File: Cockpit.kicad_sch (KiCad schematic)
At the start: 0 parts

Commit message: cockpit done
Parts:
- added C25, C27, C29, C30, C31, C32: 100nF, Capacitor_SMD:C_0603_1608Metric, symbol Device:C
- added C26, C28, C33, C34: 22pF, Capacitor_SMD:C_0603_1608Metric, symbol Device:C
- added D2: PI_DEG_A_BLUE, LED_THT:LED_D3.0mm, symbol Device:LED
- added D3: PI_DEG_B_BLUE, LED_THT:LED_D3.0mm, symbol Device:LED
- added D4: PI_ERROR_RED, LED_THT:LED_D3.0mm, symbol Device:LED
- added J2: PI_GPIO_40, Connector_PinHeader_2.54mm:PinHeader_2x20_P2.54mm_Vertical, symbol Connector_Generic:Conn_02x20_Odd_Even
- added J3: CAN_A_PROBE, Connector_PinHeader_2.54mm:PinHeader_1x02_P2.54mm_Vertical, symbol Connector_Generic:Conn_01x02
- added J4: CAN_B_PROBE, Connector_PinHeader_2.54mm:PinHeader_1x02_P2.54mm_Vertical, symbol Connector_Generic:Conn_01x02
- added R17, R18, R20, R21: 10k, Resistor_SMD:R_0603_1608Metric, symbol Device:R
- added R19, R22: 120R, Resistor_SMD:R_0603_1608Metric, symbol Device:R
- added R23, R24, R25: 220R, Resistor_SMD:R_0603_1608Metric, symbol Device:R
- added S1: PI_SELF_TEST, SWT0210-045026GSA:SW_SWT0210-045026GSA_REVA, symbol SWT0210-045026GSA:SWT0210-045026GSA_REVA
- added SW1, SW3: 219-2MSTR, Button_Switch_SMD:SW_DIP_SPSTx02_Slide_6.7x6.64mm_W8.61mm_P2.54mm_LowProfile, symbol Switch:SW_DIP_x02
- added SW2, SW4: CVS-01TB, Button_Switch_SMD:SW_DIP_SPSTx01_Slide_Copal_CVS-01xB_W5.9mm_P1mm, symbol Switch:SW_DIP_x01
- added TP1, TP10, TP11, TP12, TP2, TP3, TP4, TP5, TP6, TP7, TP8, TP9: 5015, TestPoint:TestPoint_Keystone_5015_Micro_Mini, symbol Connector:TestPoint
- added U4, U6: MCP2515T-I/ST, Package_SO:TSSOP-20_4.4x6.5mm_P0.65mm, symbol Interface_CAN_LIN:MCP2515-xST
- added U5, U7: SN65HVD230, Package_SO:SOIC-8_3.9x4.9mm_P1.27mm, symbol Interface_CAN_LIN:SN65HVD230
- added W1: 40-pin Pi GPIO ribbon cable, symbol Mechanical:Housing
- added Y1, Y2: 16 MHz, Crystal:Crystal_SMD_3225-4Pin_3.2x2.5mm, symbol Device:Crystal_GND24
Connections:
- new net: U4.1 (TXCAN), U5.1 (D)
- new net: C27.1, R17.1, U4.19 (~{RESET})
- new net: U4.2 (RXCAN), U5.4 (R)
- new net: R19.1, SW2.1
- new net: C31.1, R20.1, U6.19 (~{RESET})
- new net: D2.2 (A), R24.2
- new net: R22.1, SW4.1
- new net: D3.2 (A), R23.2
- new net: SW1.1, U5.7 (CANH)
- new net: SW1.2, U5.6 (CANL)
- new net: SW3.1, U7.7 (CANH)
- new net: SW3.2, U7.6 (CANL)
- new net: U6.1 (TXCAN), U7.1 (D)
- new net: U6.2 (RXCAN), U7.4 (R)
- new net: R18.2, U5.8 (Rs)
- new net: R21.2, U7.8 (Rs)
- new net: D4.2 (A), R25.2
- new net 3V3: C25.1, C29.1, C30.1, C32.1, R17.2, R20.2, U4.20 (VDD), U5.3 (VCC), U6.20 (VDD), U7.3 (VCC)
- new net 5V: J2.2 (Pin_2), J2.4 (Pin_4)
- new net CANH_A: R19.2, SW1.4
- new net CANH_B: J4.1 (Pin_1), R22.2, SW3.4
- new net CANL_A: SW1.3, SW2.2
- new net CANL_B: J4.2 (Pin_2), SW3.3, SW4.2
- new net CAN_RX_A: J2.35 (Pin_35), TP6.1
- new net CAN_RX_B: J2.36 (Pin_36), TP8.1
- new net CAN_TX_A: J2.32 (Pin_32), TP7.1
- new net CAN_TX_B: J2.33 (Pin_33), TP5.1
- new net CMD_TX: J2.31 (Pin_31), TP4.1
- new net GND: C25.2, C26.2, C27.2, C28.2, C29.2, C30.2, C31.2, C32.2, C33.2, C34.2, D2.1 (K), D3.1 (K), D4.1 (K), J2.14 (Pin_14), J2.20 (Pin_20), J2.25 (Pin_25), J2.30 (Pin_30), J2.34 (Pin_34), J2.39 (Pin_39), J2.6 (Pin_6), J2.9 (Pin_9), R18.1, R21.1, S1.1, TP1.1, TP2.1, U4.10 (VSS), U5.2 (GND), U6.10 (VSS), U7.2 (GND), Y1.2 (G), Y1.4 (G), Y2.2 (G), Y2.4 (G)
- new net OSC_PI_A1: C26.1, U4.9 (OSC1), Y1.1
- new net OSC_PI_A2: C28.1, U4.8 (OSC2), Y1.3
- new net OSC_PI_B1: C33.1, U6.8 (OSC2), Y2.1
- new net OSC_PI_B2: C34.1, U6.9 (OSC1), Y2.3
- new net PI_CAN_A_CS: J2.24 (Pin_24), U4.18 (~{CS})
- new net PI_CAN_A_INT: J2.22 (Pin_22), U4.13 (~{INT})
- new net PI_CAN_B_CS: J2.26 (Pin_26), U6.18 (~{CS})
- new net PI_CAN_B_INT: J2.18 (Pin_18), U6.13 (~{INT})
- new net PI_DEG_A_LED: J2.13 (Pin_13), R24.1, TP9.1
- new net PI_DEG_B_LED: J2.15 (Pin_15), R23.1, TP10.1
- new net PI_ERR_LED: J2.16 (Pin_16), R25.1, TP11.1
- new net PI_SELF_TEST: J2.11 (Pin_11), S1.3, TP12.1
- new net PI_SPI_MISO: J2.21 (Pin_21), U4.17 (SO), U6.17 (SO)
- new net PI_SPI_MOSI: J2.19 (Pin_19), U4.16 (SI), U6.16 (SI)
- new net PI_SPI_SCLK: J2.23 (Pin_23), U4.14 (SCK), U6.14 (SCK)
- new net UDP_RX: J2.29 (Pin_29), TP3.1
- no-connect marks 0 -> 29
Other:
- note added: "Battery Input"
- note added: "CAN A Interface"
- note added: "CAN B Interface"
- note added: "Only one probe header per CAN bus is needed."
- note added: "Pi connection: J2 connects to the Raspberry Pi 4 GPIO header using one 40-pin, 2×20 female-to-female ribbon cable. Buy Adafruit 1988, DigiKey 1528-2235-ND. Align pin 1 at both ends before powering on."
- note added: "Self Test and status LEDs"

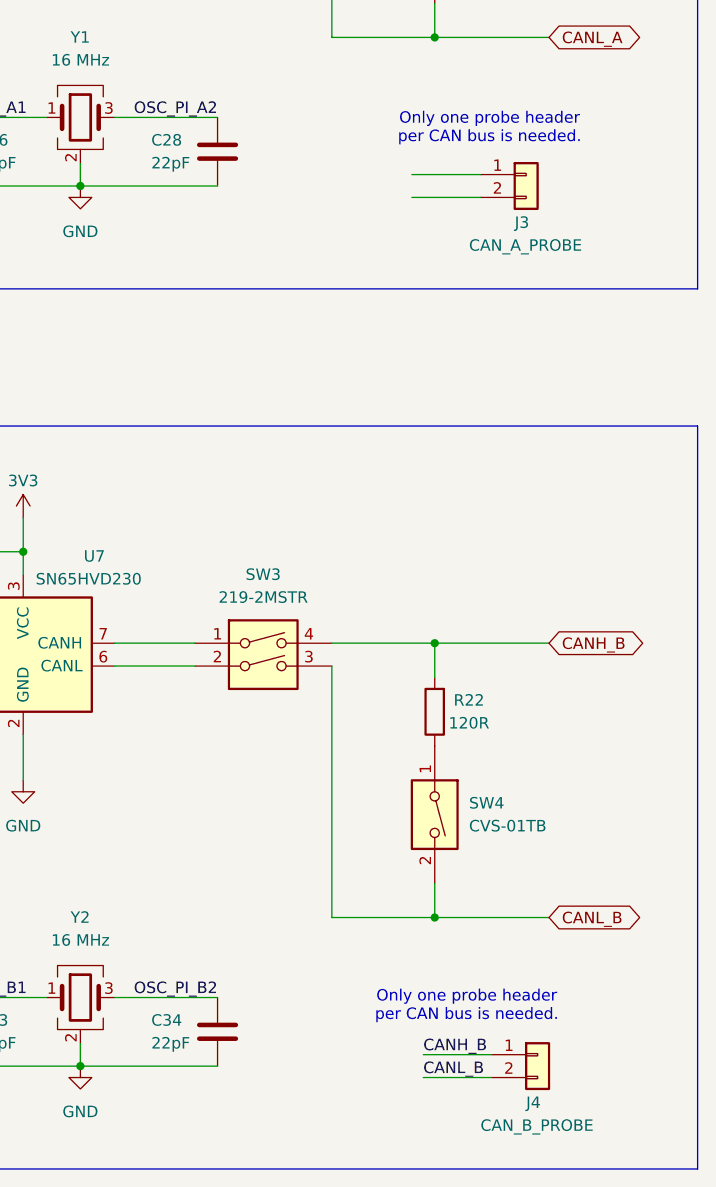
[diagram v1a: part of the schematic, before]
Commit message: Drivetrain: STM32 core, dual CAN, LEDs, self-test, test points, footprints
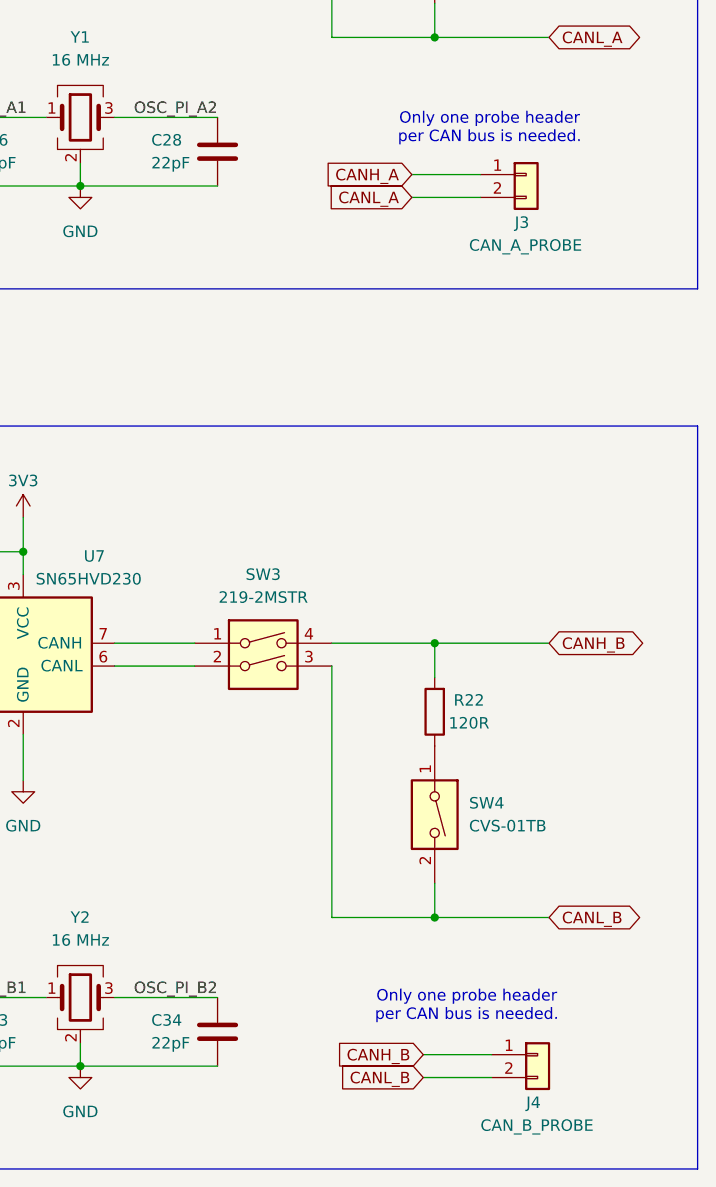
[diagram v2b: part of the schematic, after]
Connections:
- net CANH_A: now also J3.1 (Pin_1)
- net CANL_A: now also J3.2 (Pin_2)
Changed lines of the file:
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@@
-		)
-	)
-	(label "CANL_B"
-		(at 337.82 222.25 0)
-		(effects
-			(font
-				(size 1.27 1.27)
-			)
-			(justify left bottom)
 		)
 	)
@@
 	(label "CMD_TX"
 		(at 59.69 105.41 0)
-		(effects
-			(font
-				(size 1.27 1.27)
-			)
-			(justify left bottom)
-		)
-	)
-	(label "CANH_B"
-		(at 337.82 219.71 0)
 		(effects
 			(font
@@
 		)
 	)
+	(global_label "CANH_B"
+		(shape input)
+		(at 337.82 219.71 180)
+		(fields_autoplaced yes)
+		(effects
+			(font
+				(size 1.27 1.27)
+			)
+			(justify right)
+		)
+		(property "Intersheetrefs" "${INTERSHEET_REFS}"
+			(at 327.5776 219.71 0)
+			(hide yes)
+			(show_name no)
+			(do_not_autoplace no)
+			(effects
+				(font
+					(size 1.27 1.27)
+				)
+				(justify right)
+			)
+		)
+	)
 	(global_label "CANH_A"
 		(shape bidirectional)
@@
 			)
 		)
+	)
+	(global_label "CANL_B"
+		(shape input)
+		(at 337.82 222.25 180)
+		(fields_autoplaced yes)
+		(effects
+			(font
+				(size 1.27 1.27)
+			)
+			(justify right)
+		)
+		(property "Intersheetrefs" "${INTERSHEET_REFS}"
+			(at 327.88 222.25 0)
+			(hide yes)
+			(show_name no)
+			(do_not_autoplace no)
+			(effects
+				(font
+					(size 1.27 1.27)
+				)
+				(justify right)
+			)
+		)
+	)
+	(global_label "CANH_A"
+		(shape input)
+		(at 336.55 121.92 180)
+		(fields_autoplaced yes)
+		(effects
+			(font
+				(size 1.27 1.27)
+			)
+			(justify right)
+		)
+		(property "Intersheetrefs" "${INTERSHEET_REFS}"
+			(at 326.489 121.92 0)
+			(hide yes)
+			(show_name no)
+			(do_not_autoplace no)
+			(effects
+				(font
+					(size 1.27 1.27)
+				)
+				(justify right)
+			)
+		)
+	)
+	(global_label "CANL_A"
+		(shape input)
+		(at 336.55 124.46 180)
+		(fields_autoplaced yes)
+		(effects
+			(font
+				(size 1.27 1.27)
+			)
+			(justify right)
+		)
+		(property "Intersheetrefs" "${INTERSHEET_REFS}"
+			(at 326.7914 124.46 0)
+			(hide yes)
+			(show_name no)
+			(do_not_autoplace no)
+			(effects
+				(font
+					(size 1.27 1.27)
+				)
+				(justify right)
+			)
+		)

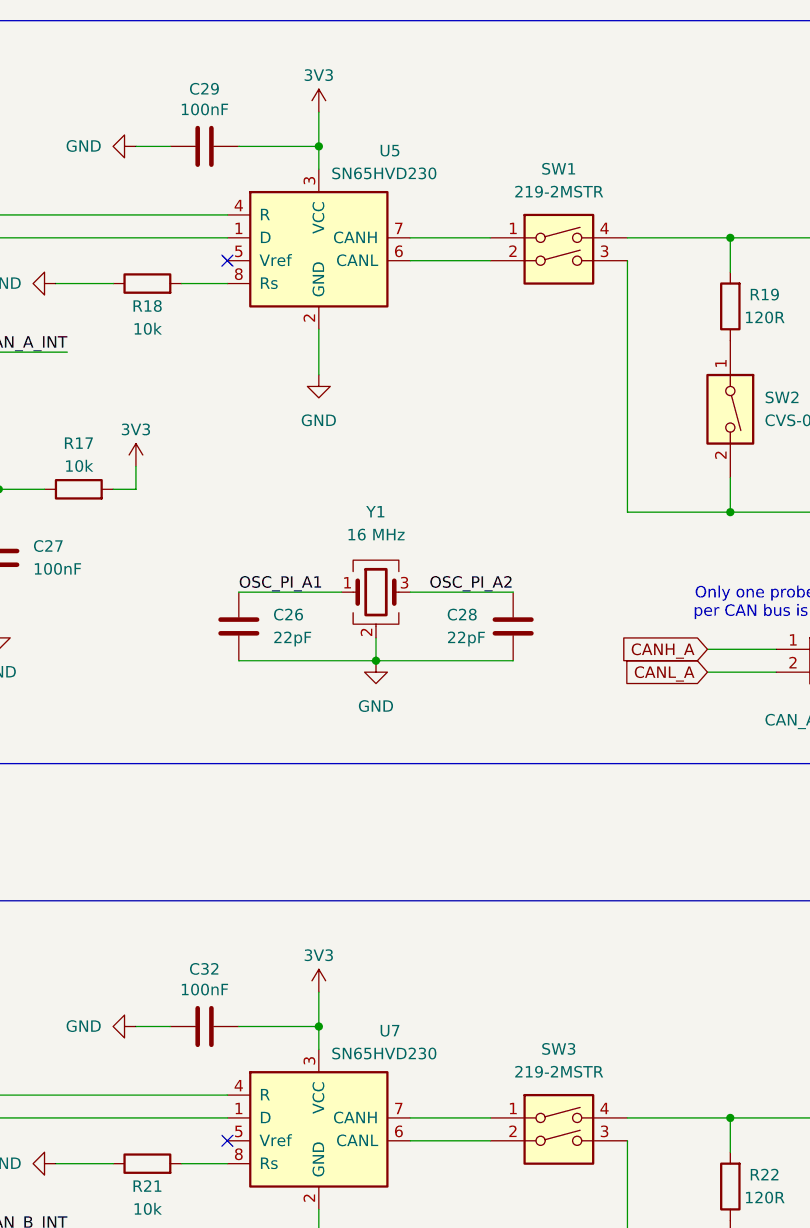
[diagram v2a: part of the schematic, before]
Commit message: changed MPN on CAN
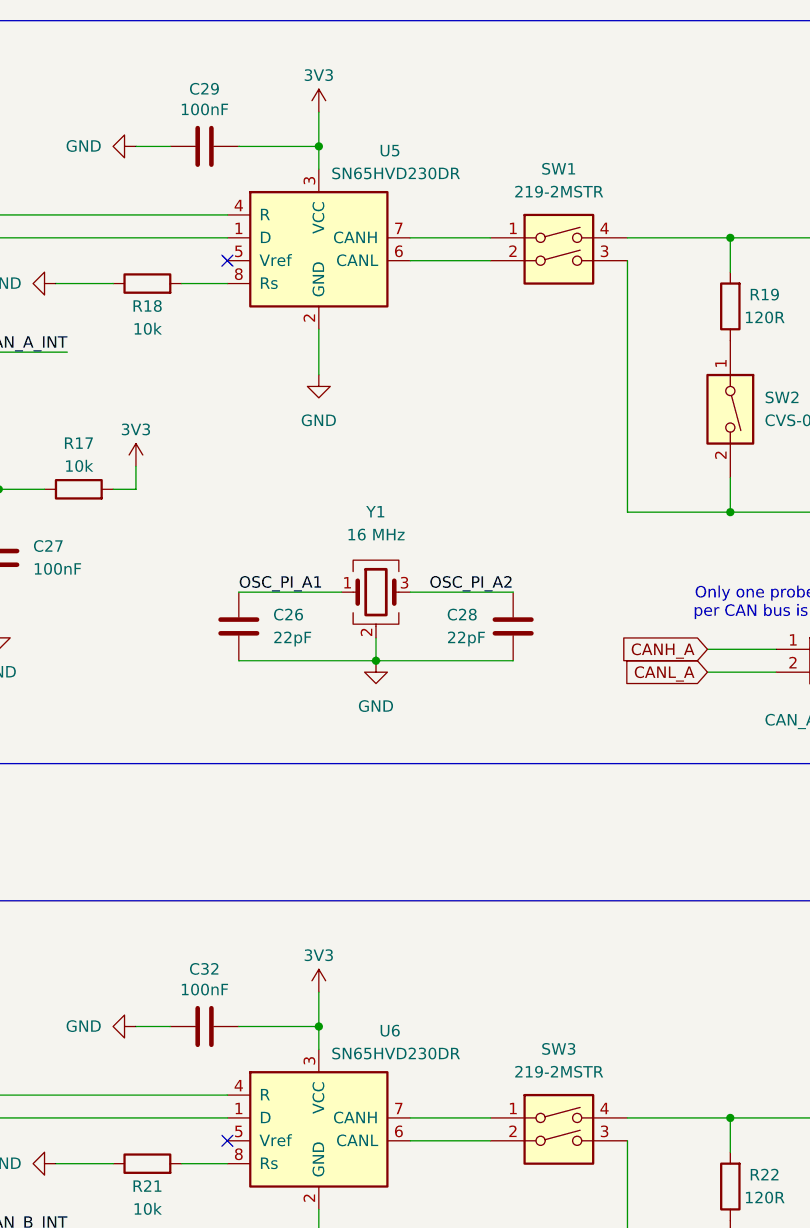
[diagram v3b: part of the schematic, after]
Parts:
- removed U7: SN65HVD230, Package_SO:SOIC-8_3.9x4.9mm_P1.27mm, symbol Interface_CAN_LIN:SN65HVD230
- added U6: SN65HVD230DR, Package_SO:SOIC-8_3.9x4.9mm_P1.27mm, symbol Interface_CAN_LIN:SN65HVD230
- U5: value SN65HVD230 -> SN65HVD230DR; Assembly (none) -> SMT; JLCPCB Category (none) -> Extended; LCSC Part # (none) -> C12084; Manufacturer (none) -> Texas Instruments; Manufacturer Part Number (none) -> SN65HVD230DR; Source (none) -> JLCPCB
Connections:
- net 3V3: now also U6.3 (VCC)
- net GND: now also U6.2 (GND)
- net at SW3.1: now also U6.7 (CANH)
- net at SW3.2: now also U6.6 (CANL)
- net at U6.1 (TXCAN): now also U6.1 (D)
- net at U6.2 (RXCAN): now also U6.4 (R)
- net at R21.2: now also U6.8 (Rs)
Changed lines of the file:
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@@
 			)
 		)
-		(property "Value" "SN65HVD230"
+		(property "Value" "SN65HVD230DR"
 			(at 294.7513 69.088 0)
 			(show_name no)
@@
 			)
 		)
-		(property "Manufacturer" ""
+		(property "Manufacturer" "Texas Instruments"
 			(at 293.37 76.2 0)
 			(hide yes)
@@
 			)
 		)
-		(property "Manufacturer Part Number" ""
+		(property "Manufacturer Part Number" "SN65HVD230DR"
 			(at 293.37 76.2 0)
 			(hide yes)
@@
 			)
 		)
-		(property "Source" ""
+		(property "Source" "JLCPCB"
 			(at 293.37 76.2 0)
 			(hide yes)
@@
 			)
 		)
-		(property "Assembly" ""
+		(property "Assembly" "SMT"
 			(at 293.37 76.2 0)
 			(hide yes)
@@
 			)
 		)
-		(property "LCSC Part #" ""
+		(property "LCSC Part #" "C12084"
 			(at 293.37 76.2 0)
 			(hide yes)
@@
 			)
 		)
-		(property "JLCPCB Category" ""
+		(property "JLCPCB Category" "Extended"
 			(at 293.37 76.2 0)
 			(hide yes)
@@
 	)
 	(symbol
+		(lib_id "Interface_CAN_LIN:SN65HVD230")
+		(at 293.37 173.99 0)
+		(unit 1)
+		(body_style 1)
+		(exclude_from_sim no)
+		(in_bom yes)
+		(on_board yes)
+		(in_pos_files yes)
+		(dnp no)
+		(property "Reference" "U6"
+			(at 300.0853 164.338 0)
+			(show_name no)
+			(do_not_autoplace no)
+			(effects
+				(font
+					(size 1.27 1.27)
+				)
+				(justify left)
+			)
+		)
+		(property "Value" "SN65HVD230DR"
+			(at 294.7513 166.878 0)
+			(show_name no)
+			(do_not_autoplace no)
+			(effects
+				(font
+					(size 1.27 1.27)
+				)
+				(justify left)
+			)
+		)
+		(property "Footprint" "Package_SO:SOIC-8_3.9x4.9mm_P1.27mm"
+			(at 293.37 186.69 0)
+			(hide yes)
+			(show_name no)
+			(do_not_autoplace no)
+			(effects
+				(font
+					(size 1.27 1.27)
+				)
+			)
+		)
+		(property "Datasheet" "http://www.ti.com/lit/ds/symlink/sn65hvd230.pdf"
+			(at 290.83 163.83 0)
+			(hide yes)
+			(show_name no)
+			(do_not_autoplace no)
+			(effects
+				(font
+					(size 1.27 1.27)
+				)
+			)
+		)
+		(property "Description" "CAN Bus Transceivers, 3.3V, 1Mbps, Low-Power capabilities, SOIC-8"
+			(at 293.37 173.99 0)
+			(hide yes)
+			(show_name no)
+			(do_not_autoplace no)
+			(effects
+				(font
+					(size 1.27 1.27)
+				)
+			)
+		)
+		(property "Manufacturer" "Texas Instruments"
+			(at 293.37 173.99 0)
+			(hide yes)
+			(show_name no)
+			(do_not_autoplace no)
+			(effects
+				(font
+					(size 1.27 1.27)
+				)
+			)
+		)
+		(property "Manufacturer Part Number" "SN65HVD230DR"
+			(at 293.37 173.99 0)
+			(hide yes)
+			(show_name no)
+			(do_not_autoplace no)
+			(effects
+				(font
+					(size 1.27 1.27)
+				)
+			)
+		)
+		(property "Source" "JLCPCB"
+			(at 293.37 173.99 0)
+			(hide yes)
+			(show_name no)
+			(do_not_autoplace no)
+			(effects
+				(font
+					(size 1.27 1.27)
+				)
+			)
+		)
+		(property "Assembly" "SMT"
+			(at 293.37 173.99 0)
+			(hide yes)
+			(show_name no)
+			(do_not_autoplace no)
+			(effects
+				(font
+					(size 1.27 1.27)
+				)
+			)
+		)
+		(property "LCSC Part #" "C12084"
+			(at 293.37 173.99 0)
+			(hide yes)
+			(show_name no)
+			(do_not_autoplace no)
+			(effects
+				(font
+					(size 1.27 1.27)
+				)
+			)
+		)
+		(property "JLCPCB Category" "Extended"
+			(at 293.37 173.99 0)
+			(hide yes)
+			(show_name no)
+			(do_not_autoplace no)
+			(effects
+				(font
+					(size 1.27 1.27)
+				)
+			)
+		)
+		(pin "1"
+		)
+		(pin "6"
+		)
+		(pin "4"
+		)
+		(pin "8"
+		)
+		(pin "5"
+		)
+		(pin "3"
+		)
+		(pin "2"
+		)
+		(pin "7"
+		)
+		(instances
+			(project "pcb_lab"
+				(path "/4b3900cd-4caa-4607-9ae2-b7ba504fedd7/400b9cda-173c-4c6c-b07d-ad4608bdfc14"
+					(reference "U6")
+					(unit 1)
+				)
+			)
+		)
+	)
+	(symbol
 		(lib_id "Connector:TestPoint")
 		(at 110.49 187.96 180)
@@
 					(unit 1)
 				)
-			)
-		)
-	)
-	(symbol
-		(lib_id "Interface_CAN_LIN:SN65HVD230")
-		(at 293.37 173.99 0)
-		(unit 1)
-		(body_style 1)
-		(exclude_from_sim no)
-		(in_bom yes)
-		(on_board yes)
-		(in_pos_files yes)
-		(dnp no)
-		(property "Reference" "U7"
-			(at 300.0853 164.338 0)
-			(show_name no)
-			(do_not_autoplace no)
-			(effects
-				(font
-					(size 1.27 1.27)
-				)
-				(justify left)
-			)
-		)
-		(property "Value" "SN65HVD230"
-			(at 294.7513 166.878 0)
-			(show_name no)
-			(do_not_autoplace no)
-			(effects
-				(font
-					(size 1.27 1.27)
-				)
-				(justify left)
-			)
-		)
-		(property "Footprint" "Package_SO:SOIC-8_3.9x4.9mm_P1.27mm"
-			(at 293.37 186.69 0)
-			(hide yes)
-			(show_name no)
-			(do_not_autoplace no)
-			(effects
-				(font
-					(size 1.27 1.27)
-				)
-			)
-		)
-		(property "Datasheet" "http://www.ti.com/lit/ds/symlink/sn65hvd230.pdf"
-			(at 290.83 163.83 0)
-			(hide yes)
-			(show_name no)
-			(do_not_autoplace no)
-			(effects
-				(font
-					(size 1.27 1.27)
-				)
-			)
-		)
-		(property "Description" "CAN Bus Transceivers, 3.3V, 1Mbps, Low-Power capabilities, SOIC-8"
-			(at 293.37 173.99 0)
-			(hide yes)
-			(show_name no)
-			(do_not_autoplace no)
-			(effects
-				(font
-					(size 1.27 1.27)
-				)
-			)
-		)
-		(property "Manufacturer" ""
-			(at 293.37 173.99 0)
-			(hide yes)
-			(show_name no)
-			(do_not_autoplace no)
-			(effects
-				(font
-					(size 1.27 1.27)
-				)
-			)
-		)
-		(property "Manufacturer Part Number" ""
-			(at 293.37 173.99 0)
-			(hide yes)
-			(show_name no)
-			(do_not_autoplace no)
-			(effects
-				(font
-					(size 1.27 1.27)
-				)
-			)
-		)
-		(property "Source" ""
-			(at 293.37 173.99 0)
-			(hide yes)
-			(show_name no)
-			(do_not_autoplace no)
-			(effects
-				(font
-					(size 1.27 1.27)
-				)
-			)
-		)
-		(property "Assembly" ""
-			(at 293.37 173.99 0)
-			(hide yes)
-			(show_name no)
-			(do_not_autoplace no)
-			(effects
-				(font
-					(size 1.27 1.27)
-				)
-			)
-		)
-		(property "LCSC Part #" ""
-			(at 293.37 173.99 0)
-			(hide yes)
-			(show_name no)
-			(do_not_autoplace no)
-			(effects
-				(font
-					(size 1.27 1.27)
-				)
-			)
-		)
-		(property "JLCPCB Category" ""
-			(at 293.37 173.99 0)
-			(hide yes)
-			(show_name no)
-			(do_not_autoplace no)
-			(effects
-				(font
-					(size 1.27 1.27)
-				)
-			)
-		)
-		(pin "1"
-		)
-		(pin "6"
-		)
-		(pin "4"
-		)
-		(pin "8"
-		)
-		(pin "5"
-		)
-		(pin "3"
-		)
-		(pin "2"
-		)
-		(pin "7"
-		)
-		(instances
-			(project "pcb_lab"
-				(path "/4b3900cd-4caa-4607-9ae2-b7ba504fedd7/400b9cda-173c-4c6c-b07d-ad4608bdfc14"
-					(reference "U7")
-					(unit 1)
-				)
